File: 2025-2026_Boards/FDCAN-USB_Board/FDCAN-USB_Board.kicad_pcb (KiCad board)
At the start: 2 copper layers, 50.5 x 34.8 mm, 61 parts, among them J2 Conn_01x03_Socket, J3 Conn_01x03_Socket, J4 Conn_01x03_Socket, J5 Conn_01x02_Pin, J6 Conn_ARM_JTAG_SWD_10, J7 USB4110-GF-A, U1 AMS1117-3.3, U2 USBLC6-2SC6, U3 STM32G474CETx, U4 TCAN1057AEV-Q1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

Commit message: Final Design Reupload
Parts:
- C11: value 10n -> 100n
- R10, R11, R12, R14, R15, R5, R6, R7, R8, R9: value 1k -> 220
- turned R2 to 90 degrees
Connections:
- R2 pad 1: GND -> Net-(J7-CC1)
- R2 pad 2: Net-(J7-CC1) -> GND
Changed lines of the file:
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@@
 			)
 		)
-		(property "Value" "1k"
+		(property "Value" "220"
 			(at 0 1.17 0)
 			(layer "F.Fab")
@@
 			)
 		)
-		(property "Value" "1k"
+		(property "Value" "220"
 			(at 0 1.17 0)
 			(layer "F.Fab")
@@
 		)
 	)
+	(footprint "Resistor_SMD:R_0603_1608Metric"
+		(layer "F.Cu")
+		(at 85.75 62.25 90)
+		(descr "Resistor SMD 0603 (1608 Metric), square (rectangular) end terminal, IPC-7351 nominal, (Body size source: IPC-SM-782 page 72, https://www.pcb-3d.com/wordpress/wp-content/uploads/ipc-sm-782a_amendment_1_and_2.pdf), generated with kicad-footprint-generator")
+		(tags "resistor")
+		(property "Reference" "R2"
+			(at 0 -1.43 90)
+			(layer "F.SilkS")
+			(hide yes)
+			(effects
+				(font
+					(size 1 1)
+					(thickness 0.15)
+				)
+			)
+		)
+		(property "Value" "5.1k"
+			(at 0 1.43 90)
+			(layer "F.Fab")
+			(effects
+				(font
+					(size 1 1)
+					(thickness 0.15)
+				)
+			)
+		)
+		(property "Datasheet" "~"
+			(at 0 0 90)
+			(layer "F.Fab")
+			(hide yes)
+			(effects
+				(font
+					(size 1.27 1.27)
+					(thickness 0.15)
+				)
+			)
+		)
+		(property "Description" "Resistor, US symbol"
+			(at 0 0 90)
+			(layer "F.Fab")
+			(hide yes)
+			(effects
+				(font
+					(size 1.27 1.27)
+					(thickness 0.15)
+				)
+			)
+		)
+		(property ki_fp_filters "R_*")
+		(sheetname "/USB Power/")
+		(sheetfile "USB_Power.kicad_sch")
+		(attr smd)
+		(fp_line
+			(start -0.237258 -0.5225)
+			(end 0.237258 -0.5225)
+			(stroke
+				(width 0.12)
+				(type solid)
+			)
+			(layer "F.SilkS")
+		)
+		(fp_line
+			(start -0.237258 0.5225)
+			(end 0.237258 0.5225)
+			(stroke
+				(width 0.12)
+				(type solid)
+			)
+			(layer "F.SilkS")
+		)
+		(fp_line
+			(start 1.48 -0.73)
+			(end 1.48 0.73)
+			(stroke
+				(width 0.05)
+				(type solid)
+			)
+			(layer "F.CrtYd")
+		)
+		(fp_line
+			(start -1.48 -0.73)
+			(end 1.48 -0.73)
+			(stroke
+				(width 0.05)
+				(type solid)
+			)
+			(layer "F.CrtYd")
+		)
+		(fp_line
+			(start 1.48 0.73)
+			(end -1.48 0.73)
+			(stroke
+				(width 0.05)
+				(type solid)
+			)
+			(layer "F.CrtYd")
+		)
+		(fp_line
+			(start -1.48 0.73)
+			(end -1.48 -0.73)
+			(stroke
+				(width 0.05)
+				(type solid)
+			)
+			(layer "F.CrtYd")
+		)
+		(fp_line
+			(start 0.8 -0.4125)
+			(end 0.8 0.4125)
+			(stroke
+				(width 0.1)
+				(type solid)
+			)
+			(layer "F.Fab")
+		)
+		(fp_line
+			(start -0.8 -0.4125)
+			(end 0.8 -0.4125)
+			(stroke
+				(width 0.1)
+				(type solid)
+			)
+			(layer "F.Fab")
+		)
+		(fp_line
+			(start 0.8 0.4125)
+			(end -0.8 0.4125)
+			(stroke
+				(width 0.1)
+				(type solid)
+			)
+			(layer "F.Fab")
+		)
+		(fp_line
+			(start -0.8 0.4125)
+			(end -0.8 -0.4125)
+			(stroke
+				(width 0.1)
+				(type solid)
+			)
+			(layer "F.Fab")
+		)
+		(fp_text user "${REFERENCE}"
+			(at 0 0 90)
+			(layer "F.Fab")
+			(effects
+				(font
+					(size 0.4 0.4)
+					(thickness 0.06)
+				)
+			)
+		)
+		(pad "1" smd roundrect
+			(at -0.825 0 90)
+			(size 0.8 0.95)
+			(layers "F.Cu" "F.Mask" "F.Paste")
+			(roundrect_rratio 0.25)
+			(net 22 "Net-(J7-CC1)")
+			(pintype "passive")
+		)
+		(pad "2" smd roundrect
+			(at 0.825 0 90)
+			(size 0.8 0.95)
+			(layers "F.Cu" "F.Mask" "F.Paste")
+			(roundrect_rratio 0.25)
+			(net 1 "GND")
+			(pintype "passive")
+		)
+		(embedded_fonts no)
+		(model "${KICAD9_3DMODEL_DIR}/Resistor_SMD.3dshapes/R_0603_1608Metric.step"
+			(offset
+				(xyz 0 0 0)
+			)
+			(scale
+				(xyz 1 1 1)
+			)
+			(rotate
+				(xyz 0 0 0)
+			)
+		)
+	)
 	(footprint "Resistor_SMD:R_0402_1005Metric"
 		(layer "F.Cu")
@@
 			)
 		)
-		(property "Value" "1k"
+		(property "Value" "220"
 			(at 0 1.17 0)
 			(layer "F.Fab")
@@
 			)
 		)
-		(property "Value" "1k"
+		(property "Value" "220"
 			(at 0 1.17 0)
 			(layer "F.Fab")
@@
 		)
 	)
-	(footprint "Resistor_SMD:R_0603_1608Metric"
-		(layer "F.Cu")
-		(at 85.75 62.29375 -90)
-		(descr "Resistor SMD 0603 (1608 Metric), square (rectangular) end terminal, IPC-7351 nominal, (Body size source: IPC-SM-782 page 72, https://www.pcb-3d.com/wordpress/wp-content/uploads/ipc-sm-782a_amendment_1_and_2.pdf), generated with kicad-footprint-generator")
-		(tags "resistor")
-		(property "Reference" "R2"
-			(at 0 -1.43 90)
-			(layer "F.SilkS")
-			(hide yes)
-			(effects
-				(font
-					(size 1 1)
-					(thickness 0.15)
-				)
-			)
-		)
-		(property "Value" "5.1k"
-			(at 0 1.43 90)
-			(layer "F.Fab")
-			(hide yes)
-			(effects
-				(font
-					(size 1 1)
-					(thickness 0.15)
-				)
-			)
-		)
-		(property "Datasheet" "~"
-			(at 0 0 90)
-			(layer "F.Fab")
-			(hide yes)
-			(effects
-				(font
-					(size 1.27 1.27)
-					(thickness 0.15)
-				)
-			)
-		)
-		(property "Description" "Resistor, US symbol"
-			(at 0 0 90)
-			(layer "F.Fab")
-			(hide yes)
-			(effects
-				(font
-					(size 1.27 1.27)
-					(thickness 0.15)
-				)
-			)
-		)
-		(property ki_fp_filters "R_*")
-		(sheetname "/USB Power/")
-		(sheetfile "USB_Power.kicad_sch")
-		(attr smd)
-		(fp_line
-			(start -0.237258 0.5225)
-			(end 0.237258 0.5225)
-			(stroke
-				(width 0.12)
-				(type solid)
-			)
-			(layer "F.SilkS")
-		)
-		(fp_line
-			(start -0.237258 -0.5225)
-			(end 0.237258 -0.5225)
-			(stroke
-				(width 0.12)
-				(type solid)
-			)
-			(layer "F.SilkS")
-		)
-		(fp_line
-			(start -1.48 0.73)
-			(end -1.48 -0.73)
-			(stroke
-				(width 0.05)
-				(type solid)
-			)
-			(layer "F.CrtYd")
-		)
-		(fp_line
-			(start 1.48 0.73)
-			(end -1.48 0.73)
-			(stroke
-				(width 0.05)
-				(type solid)
-			)
-			(layer "F.CrtYd")
-		)
-		(fp_line
-			(start -1.48 -0.73)
-			(end 1.48 -0.73)
-			(stroke
-				(width 0.05)
-				(type solid)
-			)
-			(layer "F.CrtYd")
-		)
-		(fp_line
-			(start 1.48 -0.73)
-			(end 1.48 0.73)
-			(stroke
-				(width 0.05)
-				(type solid)
-			)
-			(layer "F.CrtYd")
-		)
-		(fp_line
-			(start -0.8 0.4125)
-			(end -0.8 -0.4125)
-			(stroke
-				(width 0.1)
-				(type solid)
-			)
-			(layer "F.Fab")
-		)
-		(fp_line
-			(start 0.8 0.4125)
-			(end -0.8 0.4125)
-			(stroke
-				(width 0.1)
-				(type solid)
-			)
-			(layer "F.Fab")
-		)
-		(fp_line
-			(start -0.8 -0.4125)
-			(end 0.8 -0.4125)
-			(stroke
-				(width 0.1)
-				(type solid)
-			)
-			(layer "F.Fab")
-		)
-		(fp_line
-			(start 0.8 -0.4125)
-			(end 0.8 0.4125)
-			(stroke
-				(width 0.1)
-				(type solid)
-			)
-			(layer "F.Fab")
-		)
-		(fp_text user "${REFERENCE}"
-			(at 0 0 90)
-			(layer "F.Fab")
-			(effects
-				(font
-					(size 0.4 0.4)
-					(thickness 0.06)
-				)
-			)
-		)
-		(pad "1" smd roundrect
-			(at -0.825 0 270)
-			(size 0.8 0.95)
-			(layers "F.Cu" "F.Mask" "F.Paste")
-			(roundrect_rratio 0.25)
-			(net 1 "GND")
-			(pintype "passive")
-		)
-		(pad "2" smd roundrect
-			(at 0.825 0 270)
-			(size 0.8 0.95)
-			(layers "F.Cu" "F.Mask" "F.Paste")
-			(roundrect_rratio 0.25)
-			(net 22 "Net-(J7-CC1)")
-			(pintype "passive")
-		)
-		(embedded_fonts no)
-		(model "${KICAD9_3DMODEL_DIR}/Resistor_SMD.3dshapes/R_0603_1608Metric.step"
-			(offset
-				(xyz 0 0 0)
-			)
-			(scale
-				(xyz 1 1 1)
-			)
-			(rotate
-				(xyz 0 0 0)
-			)
-		)
-	)
 	(footprint "Capacitor_SMD:C_0402_1005Metric"
 		(layer "F.Cu")
@@
 			)
 		)
-		(property "Value" "1k"
+		(property "Value" "220"
 			(at 0 1.17 0)
 			(layer "F.Fab")
@@
 			)
 		)
-		(property "Value" "1k"
+		(property "Value" "220"
 			(at 0 1.17 90)
 			(layer "F.Fab")
@@
 			)
 		)
-		(property "Value" "1k"
+		(property "Value" "220"
 			(at 0 1.17 90)
 			(layer "F.Fab")
@@
 			)
 		)
-		(property "Value" "1k"
+		(property "Value" "220"
 			(at 0 1.17 90)
 			(layer "F.Fab")
@@
 			)
 		)
-		(property "Value" "1k"
+		(property "Value" "220"
 			(at 0 1.17 0)
 			(layer "F.Fab")
@@
 			)
 		)
-		(property "Value" "1k"
+		(property "Value" "220"
 			(at 0 1.17 0)
 			(layer "F.Fab")
@@
 			)
 		)
-		(property "Value" "10n"
+		(property "Value" "100n"
 			(at 0 1.16 90)
 			(layer "F.Fab")

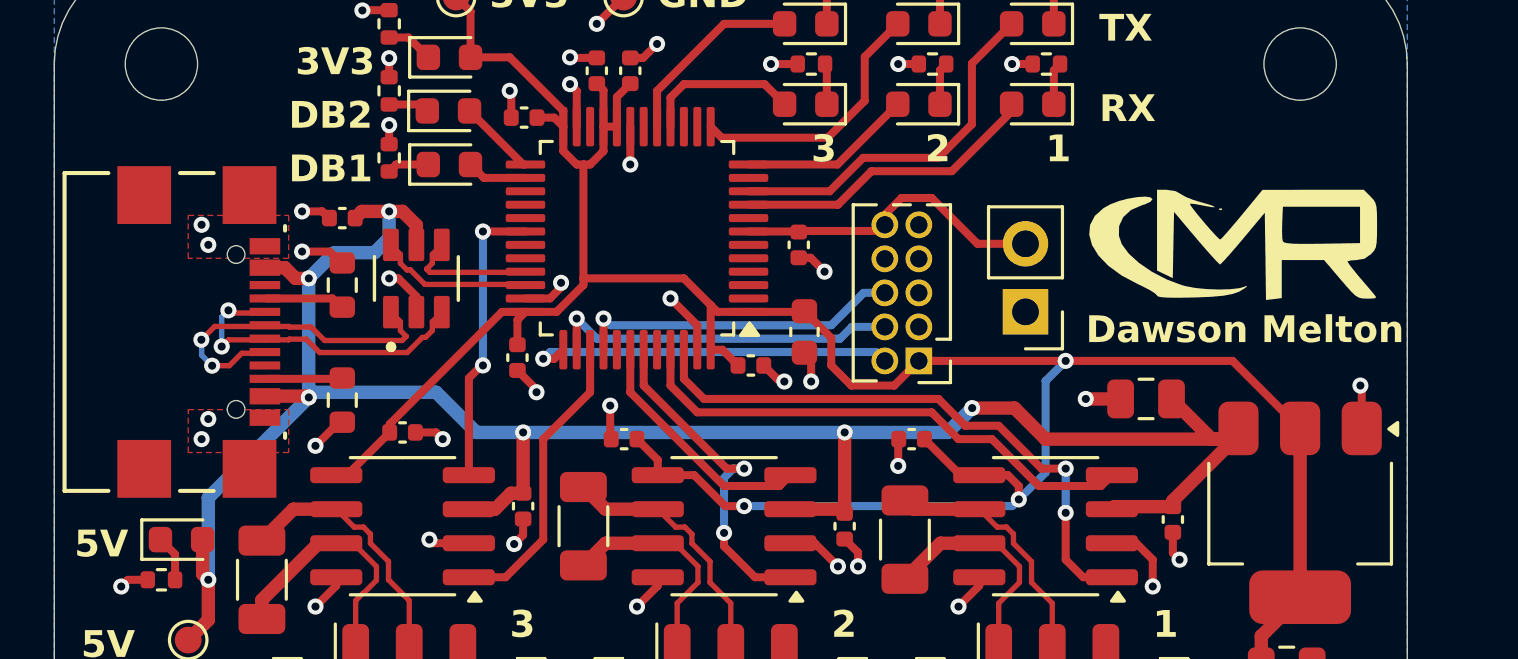
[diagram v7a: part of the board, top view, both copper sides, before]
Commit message: USB swap and updated BOM
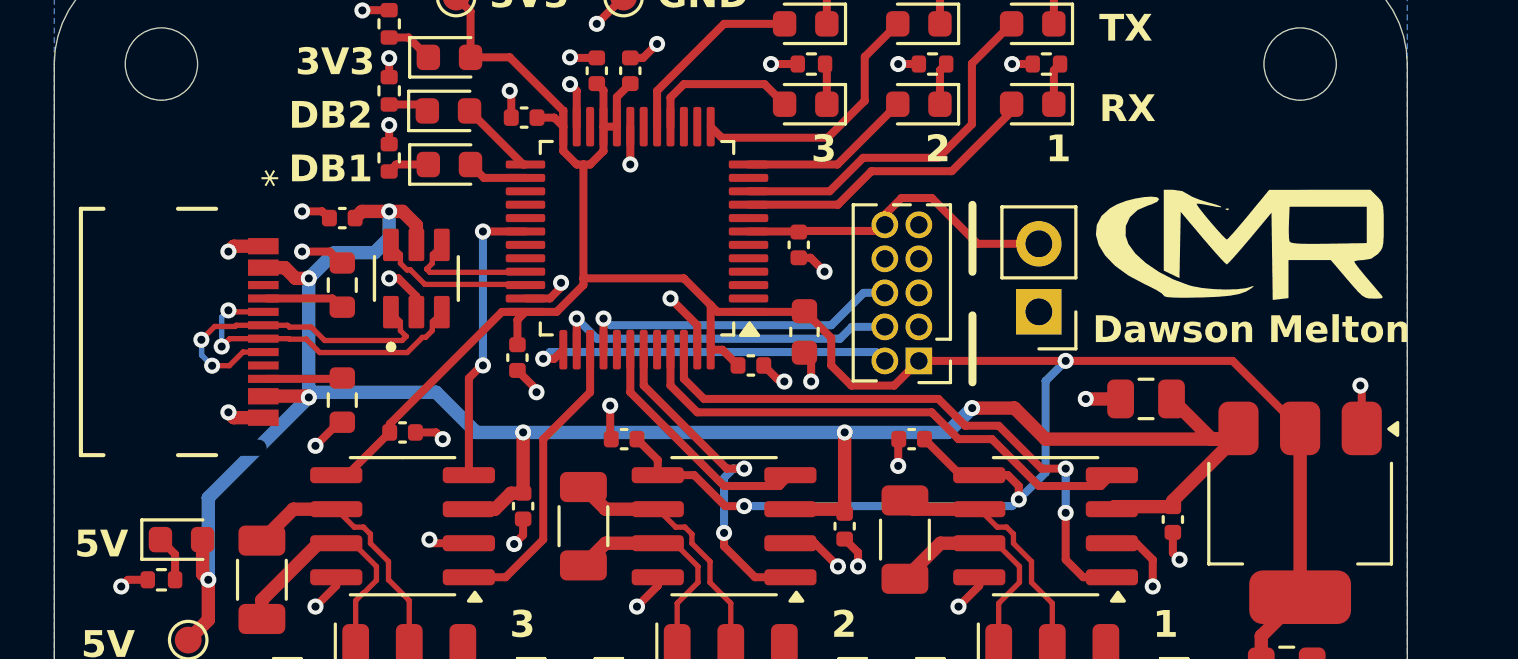
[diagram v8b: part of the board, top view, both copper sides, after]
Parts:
- removed J7: USB4110-GF-A, Cornell_Mars_Rover:USB4110-GF-A_GCT
- added J1: 2171790001, Cornell_Mars_Rover:2171790001_MOL, F.Cu at (79.5, 64.0)
- moved J5 0.50 mm to (111.8, 63.2)
- moved G*** 0.25 mm to (119.2, 61.8)
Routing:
- net GND: track 56.8 -> 59.5 mm, vias 48 -> 46
- net NRST: track 11.8 -> 12.3 mm
- removed copper zone on F.Cu, net GND
